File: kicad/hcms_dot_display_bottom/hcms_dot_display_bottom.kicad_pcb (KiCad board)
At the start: 4 copper layers, 35.5 x 39.9 mm, 56 parts, among them J1 Conn_01x12, J2 USB_C_Receptacle_USB2.0, J3 Conn_01x12, J4 Conn_01x11_Female, J5 Conn_01x11_Male, J6 Conn_01x12, J7 Conn_01x12, J8 Conn_01x02_Male, Q1 Q_PMOS_DSG, Q2 Q_PMOS_DSG, Q3 Q_PMOS_DSG, Q4 Q_PMOS_DSG, Q5 Q_PMOS_DSG, Q6 Q_PMOS_DSG, SW1 SW_DIP_x03, U1 ATtiny1626-X, U2 FT231XS

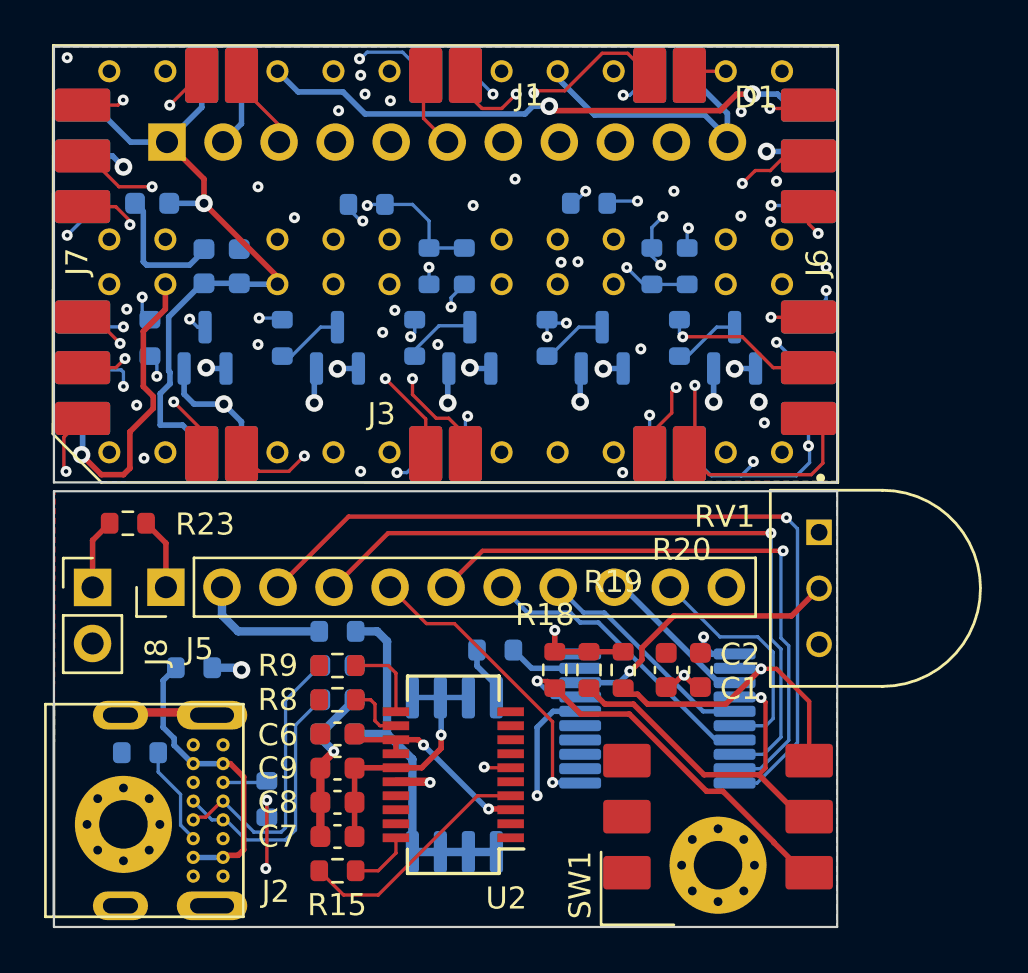
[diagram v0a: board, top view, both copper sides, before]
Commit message: progress making bottom manufacturable
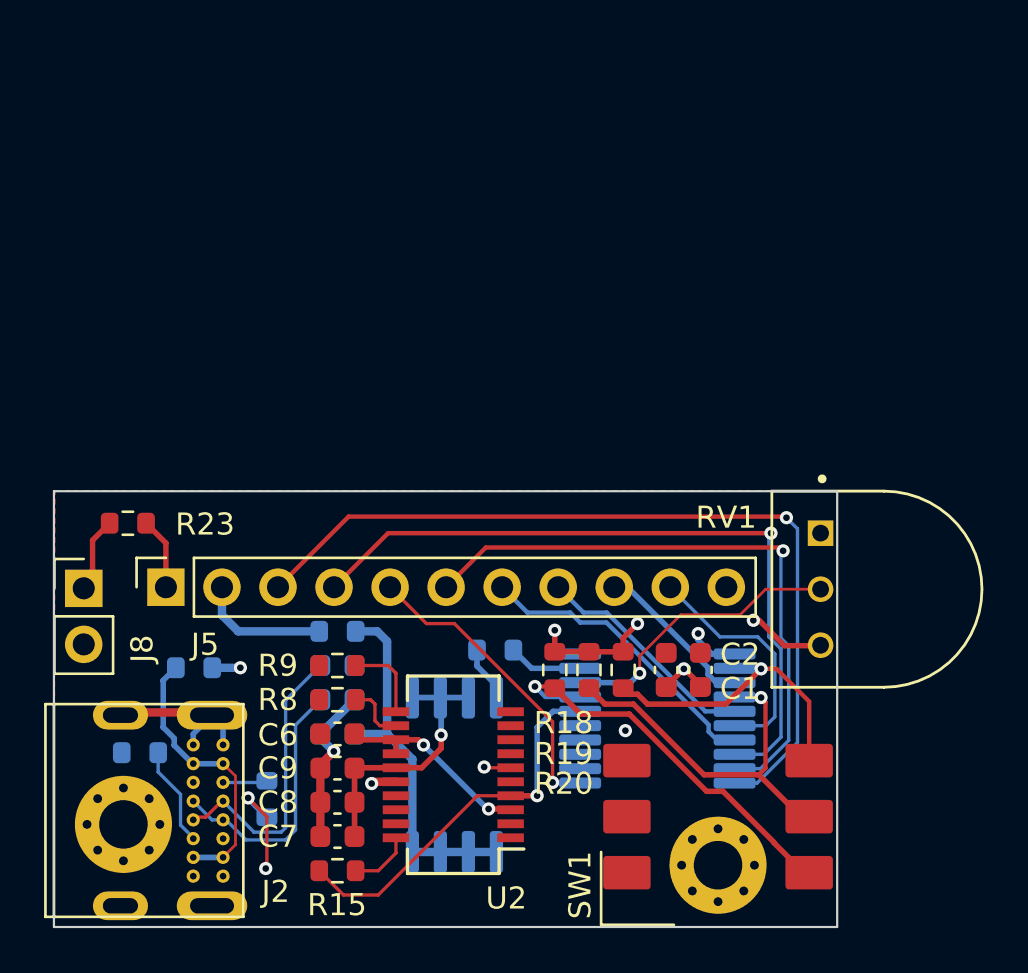
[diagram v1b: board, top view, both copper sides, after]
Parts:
- removed C10, C11: 10nF, Capacitor_SMD:C_0603_1608Metric
- removed C3: 100nF, Capacitor_SMD:C_0603_1608Metric
- removed D1: HCMS-272X, hcms:HCMS-2722
- removed J1, J3: Conn_01x12, hcms:board to board con top bot
- removed J4: Conn_01x11_Female, Connector_PinSocket_2.54mm:PinSocket_1x11_P2.54mm_Vertical
- removed J6, J7: Conn_01x12, hcms:board to board con left right
- removed Q1, Q2, Q3, Q4, Q5: Q_PMOS_DSG, Package_TO_SOT_SMD:SOT-23
- removed R1, R6: 0, Resistor_SMD:R_0603_1608Metric
- removed R10, R11, R12, R13, R14: 200, Resistor_SMD:R_0603_1608Metric
- removed R16, R17, R2, R7: DNP, Resistor_SMD:R_0603_1608Metric
- J5: value Conn_01x11_Male -> Conn_01x11_Female; footprint Connector_PinHeader_2.54mm:PinHeader_1x11_P2.54mm_Vertical -> Connector_PinSocket_2.54mm:PinSocket_1x11_P2.54mm_Vertical
- MH1, MH2: moved to B.Cu
- moved J8 0.40 mm to (164.1, 114.4)
- moved RV1 0.08 mm to (200.4, 114.4)
- turned MH1 to 180 degrees
- turned MH2 to 180 degrees
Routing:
- net /nBLNK: track 98.8 -> 10.9 mm, vias 5 -> 0
- net /CLK: track 89.7 -> 7.98 mm, vias 7 -> 0
- net /MCU_COL_1: track 85.7 -> 13.9 mm, vias 8 -> 1
- net /V_COL: track 77.7 -> 5.98 mm, vias 8 -> 0
- net /MCU_COL_4: track 103.4 -> 32.5 mm, vias 10 -> 1
- net /MCU_COL_2: track 108.1 -> 38.4 mm, vias 8 -> 1
- net /MCU_COL_3: track 95.7 -> 27.5 mm, vias 10 -> 1
- net /MCU_COL_5: track 81.2 -> 14.1 mm, vias 5 -> 0
- net +5V: track 83.0 -> 19.5 mm, vias 6 -> 4
- net /B_DATA: track 52.6 -> 0.00 mm, vias 3 -> 0
- net /A_DATA: track 45.9 -> 0.00 mm, vias 4 -> 0
- net /DAISY_B_DATA: track 37.4 -> 0.00 mm, vias 6 -> 0
- net /DAISY_A_DATA: track 35.1 -> 0.00 mm, vias 7 -> 0
- net Net-(D1-Pad26A): track 34.3 -> 0.00 mm, vias 3 -> 0
- net GND: track 66.1 -> 33.3 mm, vias 10 -> 9
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- removed copper zone on F.Cu, net GND
- removed copper zone on In1.Cu, net GND
- removed copper zone on In2.Cu, net GND
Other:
- board size 35.5 x 39.9 mm -> 35.5 x 19.8 mm
- copper layers 4 -> 2

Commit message: fuck ya
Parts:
- added G***: LOGO, LOGO, B.Cu at (185.8, 127.0)
- moved R19 0.42 mm to (186.6, 118.0)
- moved R20 0.42 mm to (188.2, 118.0)
- moved R18 0.42 mm to (185.1, 118.0)
- moved SW1 0.32 mm to (192.7, 124.5)
- moved C1 0.12 mm to (192.1, 118.0)
- moved C2 0.12 mm to (190.5, 118.0)
- moved RV1 0.11 mm to (200.3, 114.3)
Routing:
- net +5V: track 19.5 -> 25.6 mm, vias 4 -> 5
- net /CONFIG_0: track 18.2 -> 20.1 mm
- net GND: track 33.3 -> 34.6 mm
- net /CONFIG_1: track 17.0 -> 18.0 mm
- net /D+: track 13.4 -> 14.3 mm, vias 0 -> 1
- net /D-: track 12.0 -> 12.8 mm, vias 0 -> 1
- net /CONFIG_2: track 13.6 -> 14.2 mm

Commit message: easter eggs, actually ready for final review. boards passing DRC
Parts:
- added G***: LOGO, LOGO, B.Cu at (188.3, 127.4)
- moved G*** 0.32 mm to (185.9, 127.3)

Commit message: changes to bottom
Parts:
- moved RV1 0.08 mm to (200.4, 114.3)
- moved J5 0.07 mm to (167.9, 114.3)
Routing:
- net +5V: track 25.6 -> 27.1 mm
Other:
- board size 35.5 x 19.8 mm -> 35.6 x 19.8 mm
